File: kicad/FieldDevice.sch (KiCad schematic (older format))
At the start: 19 parts, among them U101 DS7505

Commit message: Altered the display connector for the DOG104 i.e. general purpose
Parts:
- D101: value LED -> Tx; symbol LED -> LED-RESCUE-FieldDevice; Link (none) -> Value
- D102: value LED -> Rx; symbol LED -> LED-RESCUE-FieldDevice
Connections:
- net 3V3: now also R112.2, R113.2
- net GND: no longer R112.1, R113.1
- net RX: now also D102.1 (K); no longer D102.2 (A)
- net TX: now also D101.1 (K); no longer D101.2 (A)
- net MISO: now reaches H101.4 (SPI_MISO/GPIO_1)
- new net: D101.2 (A), R112.1
- new net: D102.2 (A), R113.1
- no-connect marks 17 -> 16
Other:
- note added: "The minimal configuration \nfor the XBEE is Vcc, GND, \nDin and Dout"
- note removed: "# Seperate ADC for isolation away from the Micro. \n Would this be advixable/necessary?\n# Would the PTC really provide any form of protection?\n# Could a Digital Potentiometer be used here?\n# How would this really be calibrated?\n"
- note removed: "The minimal configuration for the XBEE is \nVcc, GND, DIN and DOUT"
- moved on the sheet: D101, D102, R112, R113
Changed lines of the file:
@@
 EESchema Schematic File Version 2
+LIBS:FieldDevice-rescue
 LIBS:fieldDevice_symbols
 LIBS:ce_header
@@
 Text Notes 2950 5550 0    60   ~ 0
 Temperature Sensor
-Text Notes 1050 4550 0    60   ~ 0
-# Seperate ADC for isolation away from the Micro. \n    Would this be advixable/necessary?\n# Would the PTC really provide any form of protection?\n# Could a Digital Potentiometer be used here?\n# How would this really be calibrated?\n
 Text Notes 3000 6950 0    60   ~ 0
 I²C Address '1010000'
-Text Notes 7500 1200 0    60   ~ 0
-The minimal configuration for the XBEE is \nVcc, GND, DIN and DOUT
+Text Notes 7350 1300 0    60   ~ 0
+The minimal configuration \nfor the XBEE is Vcc, GND, \nDin and Dout
 Text Label 1200 6200 0    60   ~ 0
 OverTemp
 $Sheet
-S 6650 5230 1500 1070
+S 9250 5080 1500 1070
 U 593ED75C
 F0 "Analog_Sensors" 60
 F1 "AnalogSensors.sch" 60
-F2 "ANLG_1" I L 6650 5450 60
+F2 "ANLG_1" I L 9250 5300 60
 $EndSheet
 Wire Wire Line
@@
 	650  1500 1550 1500
 Wire Wire Line
-	6650 5450 6050 5450
-Text Label 6050 5450 0    60   ~ 0
+	9250 5300 8650 5300
+Text Label 8650 5300 0    60   ~ 0
 ANLG_1
 Text Label 650  2500 0    60   ~ 0
 ANLG_1
 $Sheet
-S 6600 3700 1600 1200
+S 9200 3200 1450 1500
 U 593F4F7E
 F0 "Display" 60
 F1 "Display.sch" 60
-F2 "3V3" I L 6600 3850 60
-F3 "RS" I L 6600 4500 60
-F4 "MOSI" I L 6600 4050 60
-F5 "SPI_SCK" I L 6600 4200 60
-F6 "CS" I L 6600 4350 60
-F7 "Display" I L 6600 4750 60
+F2 "3V3" I L 9200 3350 60
+F3 "RS" I L 9200 4150 60
+F4 "MOSI" I L 9200 3550 60
+F5 "SPI_SCK" I L 9200 3850 60
+F6 "CS" I L 9200 4000 60
+F7 "Display" I L 9200 4400 60
+F8 "MISO" I L 9200 3700 60
 $EndSheet
 Wire Wire Line
-	6600 3850 6150 3850
-Wire Wire Line
-	6600 4050 6150 4050
-Wire Wire Line
-	6600 4200 6150 4200
-Wire Wire Line
-	6600 4500 6150 4500
+	9200 3350 8750 3350
+Wire Wire Line
+	9200 3550 8750 3550
+Wire Wire Line
+	9200 3850 8750 3850
+Wire Wire Line
+	9200 4150 8750 4150
 Text Label 4450 2500 2    60   ~ 0
 REG_SEL
 Wire Wire Line
-	6600 4350 6150 4350
-Text Label 6150 4350 0    60   ~ 0
+	9200 4000 8750 4000
+Text Label 8750 4000 0    60   ~ 0
 CS
-Text Label 6150 4200 0    60   ~ 0
+Text Label 8750 3850 0    60   ~ 0
 SPI_CLK
-Text Label 6150 4050 0    60   ~ 0
+Text Label 8750 3550 0    60   ~ 0
 MOSI
-Text Label 6150 3850 0    60   ~ 0
+Text Label 8750 3350 0    60   ~ 0
 3V3
 Text Label 650  1300 0    60   ~ 0
 MOSI
-NoConn ~ 3550 1300
 Wire Wire Line
 	3550 1500 4450 1500
@@
 	4000 2500 4450 2500
 Wire Wire Line
-	6600 4750 6150 4750
-Text Label 6150 4750 0    60   ~ 0
+	9200 4400 8750 4400
+Text Label 8750 4400 0    60   ~ 0
 Display
-Text Label 6150 4500 0    60   ~ 0
+Text Label 8750 4150 0    60   ~ 0
 REG_SEL
 Wire Wire Line
@@
 	5000 6200 5000 6300
 Connection ~ 5000 5800
-Text Notes 5200 5450 0    60   ~ 0
+Text Notes 8400 5500 0    60   ~ 0
 Pin 14 on Teency\ni.e. A0
 $Comp
-L LED D101
+L LED-RESCUE-FieldDevice D101
 U 1 1 59CB7CCC
-P 5500 2650
-F 0 "D101" H 5500 2750 50  0000 C CNN
-F 1 "LED" H 5500 2550 50  0000 C CNN
-F 2 "Diodes_SMD:D_0805" H 5500 2650 60  0001 C CNN
-F 3 "" H 5500 2650 60  0000 C CNN
-	1    5500 2650
+P 5500 1600
+F 0 "D101" H 5500 1700 50  0000 C CNN
+F 1 "Tx" H 5500 1500 50  0000 C CNN
+F 2 "Diodes_SMD:D_0805" H 5500 1600 60  0001 C CNN
+F 3 "" H 5500 1600 60  0000 C CNN
+F 4 "Value" H 5500 1600 60  0001 C CNN "Link"
+	1    5500 1600
 	0    -1   -1   0
 $EndComp
 $Comp
-L LED D102
+L LED-RESCUE-FieldDevice D102
 U 1 1 59CB7D69
-P 5800 2650
-F 0 "D102" H 5800 2750 50  0000 C CNN
-F 1 "LED" H 5800 2550 50  0000 C CNN
-F 2 "Diodes_SMD:D_0805" H 5800 2650 60  0001 C CNN
-F 3 "" H 5800 2650 60  0000 C CNN
-	1    5800 2650
+P 5800 1600
+F 0 "D102" H 5800 1700 50  0000 C CNN
+F 1 "Rx" H 5800 1500 50  0000 C CNN
+F 2 "Diodes_SMD:D_0805" H 5800 1600 60  0001 C CNN
+F 3 "" H 5800 1600 60  0000 C CNN
+	1    5800 1600
 	0    -1   -1   0
 $EndComp
-Wire Wire Line
-	5500 2450 5500 2000
-Connection ~ 5500 2000
-Wire Wire Line
-	5800 2450 5800 2100
-Connection ~ 5800 2100
-Wire Wire Line
-	5500 3500 5800 3500
-$Comp
-L GND #PWR07
-U 1 1 59CB7FF0
-P 5650 3750
-F 0 "#PWR07" H 5650 3500 50  0001 C CNN
-F 1 "GND" H 5650 3600 50  0000 C CNN
-F 2 "" H 5650 3750 50  0000 C CNN
-F 3 "" H 5650 3750 50  0000 C CNN
-	1    5650 3750
-	1    0    0    -1
-$EndComp
-Wire Wire Line
-	5650 3750 5650 3500
-Connection ~ 5650 3500
 $Comp
 L R R112
 U 1 1 59CB849B
-P 5500 3150
-F 0 "R112" V 5580 3150 50  0000 C CNN
-F 1 "680Ω" V 5500 3150 50  0000 C CNN
-F 2 "Resistors_SMD:R_0805_HandSoldering" V 5430 3150 50  0001 C CNN
-F 3 "" H 5500 3150 50  0000 C CNN
-	1    5500 3150
+P 5500 1050
+F 0 "R112" V 5580 1050 50  0000 C CNN
+F 1 "680Ω" V 5500 1050 50  0000 C CNN
+F 2 "Resistors_SMD:R_0805_HandSoldering" V 5430 1050 50  0001 C CNN
+F 3 "" H 5500 1050 50  0000 C CNN
+	1    5500 1050
 	-1   0    0    1
 $EndComp
@@
 L R R113
 U 1 1 59CB8725
-P 5800 3150
-F 0 "R113" V 5880 3150 50  0000 C CNN
-F 1 "680Ω" V 5800 3150 50  0000 C CNN
-F 2 "Resistors_SMD:R_0805_HandSoldering" V 5730 3150 50  0001 C CNN
-F 3 "" H 5800 3150 50  0000 C CNN
-	1    5800 3150
+P 5800 1050
+F 0 "R113" V 5880 1050 50  0000 C CNN
+F 1 "680Ω" V 5800 1050 50  0000 C CNN
+F 2 "Resistors_SMD:R_0805_HandSoldering" V 5730 1050 50  0001 C CNN
+F 3 "" H 5800 1050 50  0000 C CNN
+	1    5800 1050
 	-1   0    0    1
 $EndComp
 Wire Wire Line
-	5500 2850 5500 3000
-Wire Wire Line
-	5500 3300 5500 3500
-Wire Wire Line
-	5800 3500 5800 3300
-Wire Wire Line
-	5800 3000 5800 2850
+	5500 750  5500 900
+Wire Wire Line
+	5500 1200 5500 1400
+Wire Wire Line
+	5800 1400 5800 1200
+Wire Wire Line
+	5800 900  5800 750
+Wire Wire Line
+	5500 1800 5500 2000
+Connection ~ 5500 2000
+Wire Wire Line
+	5800 1800 5800 2100
+Connection ~ 5800 2100
+Wire Wire Line
+	5500 750  6200 750
+Connection ~ 5800 750
+Text Label 6200 750  2    60   ~ 0
+3V3
+Wire Wire Line
+	9200 3700 8750 3700
+Text Label 8750 3700 0    60   ~ 0
+MISO
+Wire Wire Line
+	3550 1300 4450 1300
+Text Label 4450 1300 2    60   ~ 0
+MISO
 $EndSCHEMATC

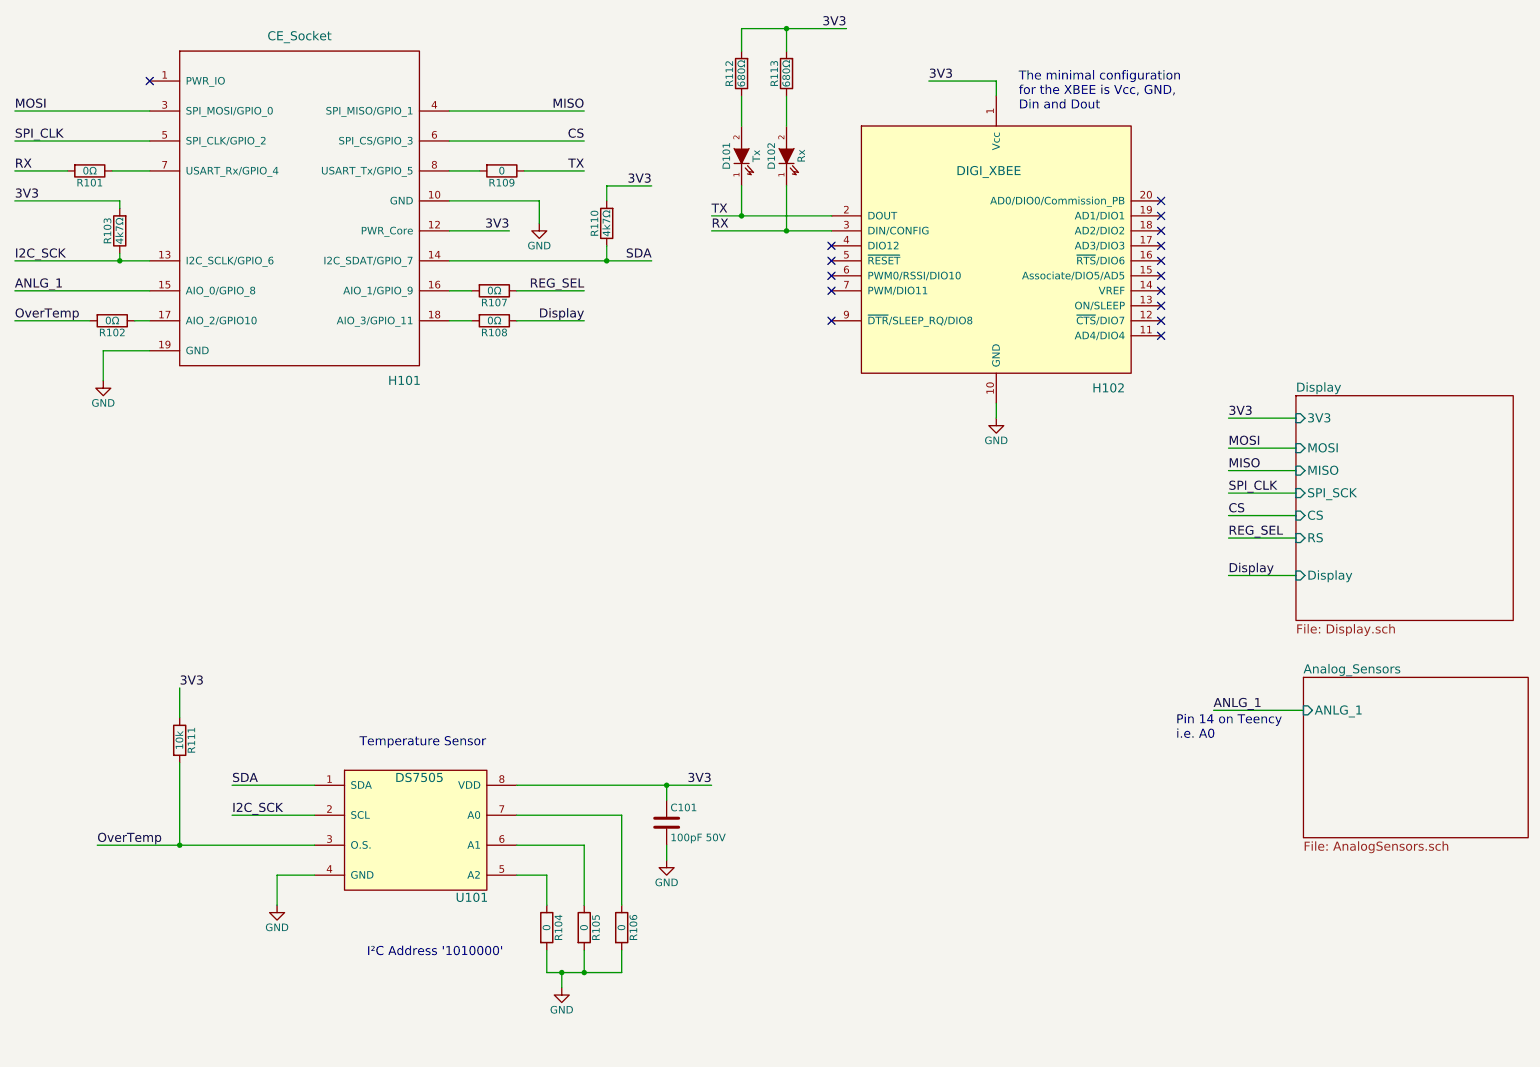
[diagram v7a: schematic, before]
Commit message: Revamping the schematic and layout for a deployable model
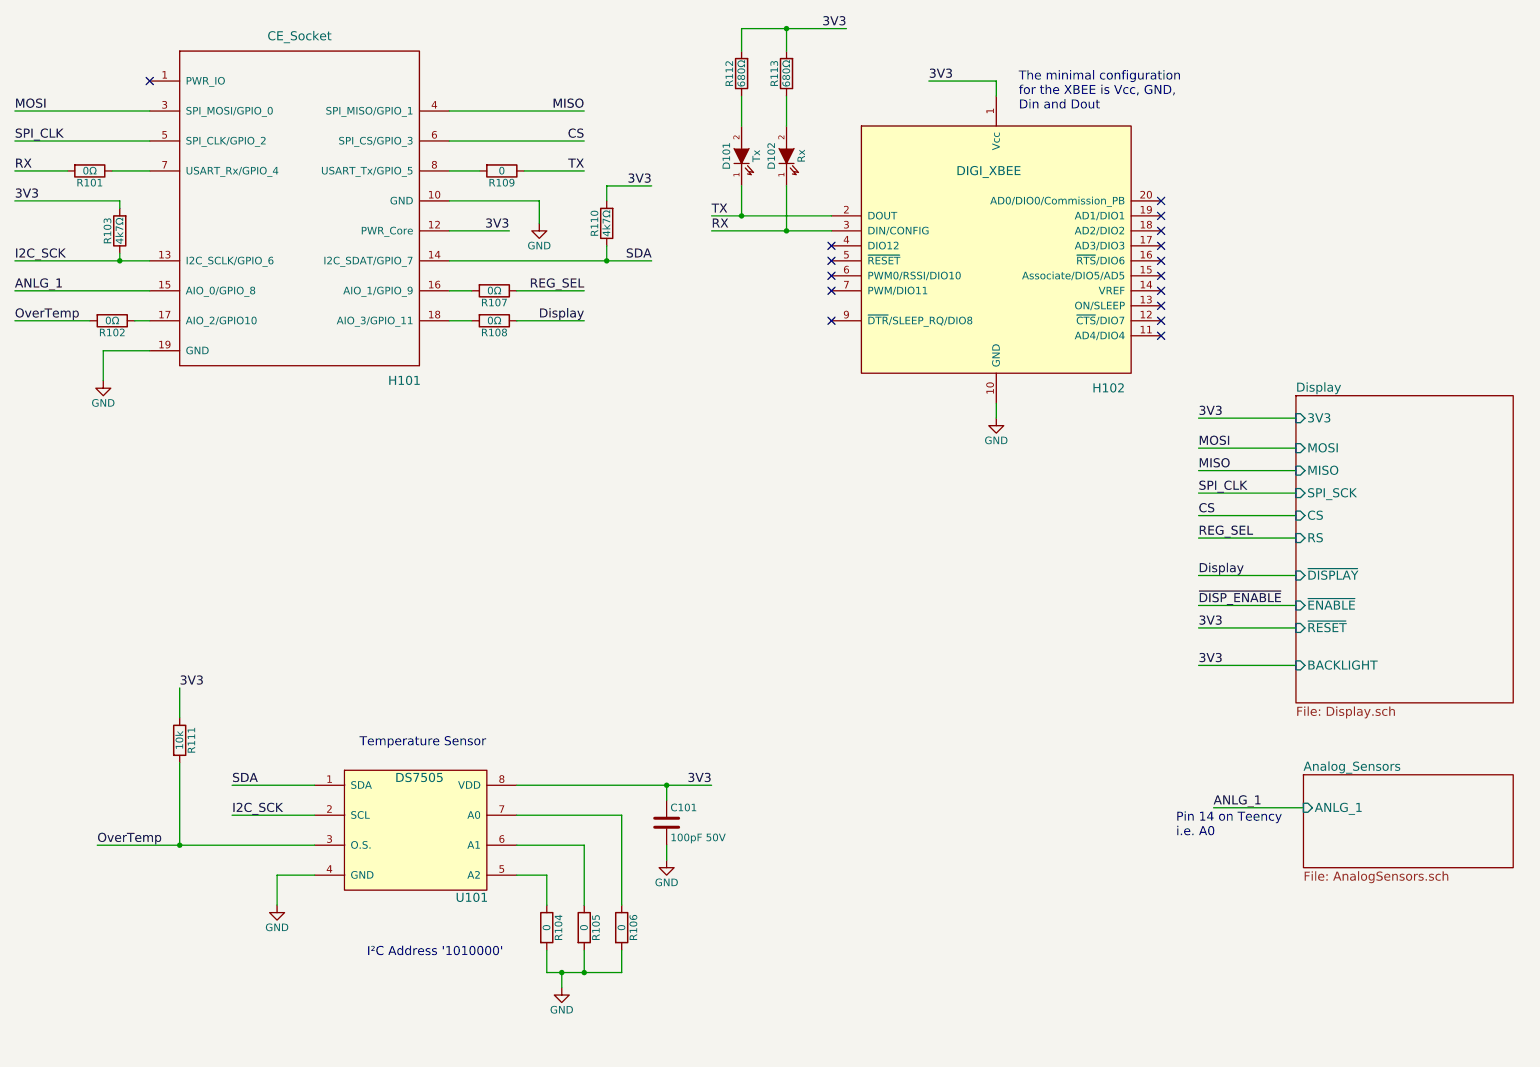
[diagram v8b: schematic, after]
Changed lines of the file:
@@
 OverTemp
 $Sheet
-S 9250 5080 1500 1070
+S 9250 5730 1400 620
 U 593ED75C
 F0 "Analog_Sensors" 60
 F1 "AnalogSensors.sch" 60
-F2 "ANLG_1" I L 9250 5300 60
+F2 "ANLG_1" I L 9250 5950 60
 $EndSheet
 Wire Wire Line
@@
 	1300 1700 1550 1700
 Wire Wire Line
-	5300 2000 6100 2000
-Wire Wire Line
-	5300 2100 6100 2100
-Wire Wire Line
-	4000 5800 5300 5800
+	5300 2000 5500 2000
+Wire Wire Line
+	5500 2000 6100 2000
+Wire Wire Line
+	5300 2100 5800 2100
+Wire Wire Line
+	5800 2100 6100 2100
+Wire Wire Line
+	4000 5800 5000 5800
+Wire Wire Line
+	5000 5800 5300 5800
 Wire Wire Line
 	2650 6400 2400 6400
@@
 	2650 6000 2100 6000
 Wire Wire Line
-	1200 6200 2650 6200
+	1200 6200 1750 6200
+Wire Wire Line
+	1750 6200 2650 6200
 Wire Wire Line
 	4200 6900 4200 7050
 Wire Wire Line
-	4200 7050 4700 7050
+	4200 7050 4300 7050
+Wire Wire Line
+	4300 7050 4450 7050
+Wire Wire Line
+	4450 7050 4700 7050
 Wire Wire Line
 	4700 7050 4700 6900
@@
 	4700 6000 4700 6600
 Wire Wire Line
-	3550 2300 4900 2300
+	3550 2300 4600 2300
+Wire Wire Line
+	4600 2300 4900 2300
 Wire Wire Line
 	7200 1100 7200 1200
@@
 	650  1500 1550 1500
 Wire Wire Line
-	9250 5300 8650 5300
-Text Label 8650 5300 0    60   ~ 0
+	9250 5950 8650 5950
+Text Label 8650 5950 0    60   ~ 0
 ANLG_1
 Text Label 650  2500 0    60   ~ 0
 ANLG_1
 $Sheet
-S 9200 3200 1450 1500
+S 9200 3200 1450 2050
 U 593F4F7E
 F0 "Display" 60
@@
 F5 "SPI_SCK" I L 9200 3850 60
 F6 "CS" I L 9200 4000 60
-F7 "Display" I L 9200 4400 60
-F8 "MISO" I L 9200 3700 60
+F7 "MISO" I L 9200 3700 60
+F8 "~RESET" I L 9200 4750 60
+F9 "BACKLIGHT" I L 9200 5000 60
+F10 "~DISPLAY" I L 9200 4400 60
+F11 "~ENABLE" I L 9200 4600 60
 $EndSheet
 Wire Wire Line
-	9200 3350 8750 3350
-Wire Wire Line
-	9200 3550 8750 3550
-Wire Wire Line
-	9200 3850 8750 3850
-Wire Wire Line
-	9200 4150 8750 4150
+	9200 3350 8550 3350
+Wire Wire Line
+	9200 3550 8550 3550
+Wire Wire Line
+	9200 3850 8550 3850
+Wire Wire Line
+	9200 4150 8550 4150
 Text Label 4450 2500 2    60   ~ 0
 REG_SEL
 Wire Wire Line
-	9200 4000 8750 4000
-Text Label 8750 4000 0    60   ~ 0
+	9200 4000 8550 4000
+Text Label 8550 4000 0    60   ~ 0
 CS
-Text Label 8750 3850 0    60   ~ 0
+Text Label 8550 3850 0    60   ~ 0
 SPI_CLK
-Text Label 8750 3550 0    60   ~ 0
+Text Label 8550 3550 0    60   ~ 0
 MOSI
-Text Label 8750 3350 0    60   ~ 0
+Text Label 8550 3350 0    60   ~ 0
 3V3
 Text Label 650  1300 0    60   ~ 0
@@
 	4000 2500 4450 2500
 Wire Wire Line
-	9200 4400 8750 4400
-Text Label 8750 4400 0    60   ~ 0
+	9200 4400 8550 4400
+Text Label 8550 4400 0    60   ~ 0
 Display
-Text Label 8750 4150 0    60   ~ 0
+Text Label 8550 4150 0    60   ~ 0
 REG_SEL
 Wire Wire Line
-	650  2300 1550 2300
+	650  2300 1350 2300
+Wire Wire Line
+	1350 2300 1550 2300
 $Comp
 L R R103
@@
 	5000 6200 5000 6300
 Connection ~ 5000 5800
-Text Notes 8400 5500 0    60   ~ 0
+Text Notes 8400 6150 0    60   ~ 0
 Pin 14 on Teency\ni.e. A0
 $Comp
@@
 Connection ~ 5800 2100
 Wire Wire Line
-	5500 750  6200 750
+	5500 750  5800 750
+Wire Wire Line
+	5800 750  6200 750
 Connection ~ 5800 750
 Text Label 6200 750  2    60   ~ 0
 3V3
 Wire Wire Line
-	9200 3700 8750 3700
-Text Label 8750 3700 0    60   ~ 0
+	9200 3700 8550 3700
+Text Label 8550 3700 0    60   ~ 0
 MISO
 Wire Wire Line
@@
 Text Label 4450 1300 2    60   ~ 0
 MISO
+Wire Wire Line
+	9200 4750 8550 4750
+Wire Wire Line
+	9200 5000 8550 5000
+Text Label 8550 4750 0    60   ~ 0
+3V3
+Text Label 8550 5000 0    60   ~ 0
+3V3
+Wire Wire Line
+	9200 4600 8550 4600
+Text Label 8550 4600 0    60   ~ 0
+~DISP_ENABLE
 $EndSCHEMATC
